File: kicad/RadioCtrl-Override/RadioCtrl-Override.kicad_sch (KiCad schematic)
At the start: 18 parts, among them J1 FW/BK/CON, J2 LF/RI/CON, J3 PJ-002AH, J5 HM10, J6 WRITER, Q1 2SC1815, Q2 2SC1815, Q3 2SC1815, Q4 2SC1815, U1 PIC16F1827-E/P

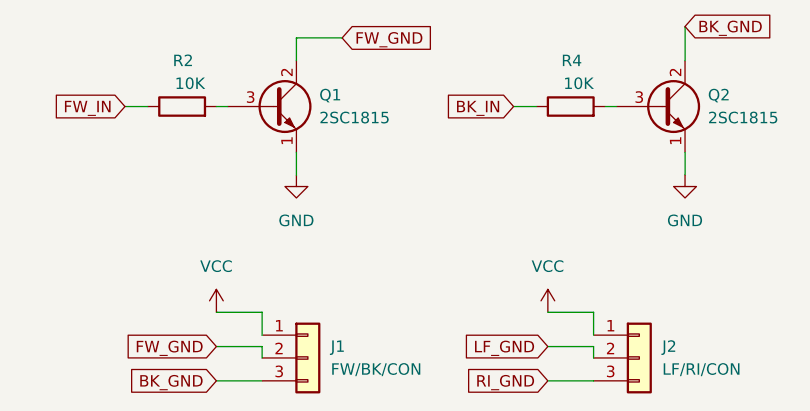
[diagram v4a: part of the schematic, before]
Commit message: 基盤の内容を修正
ターミナルのVCCをGNDに変更
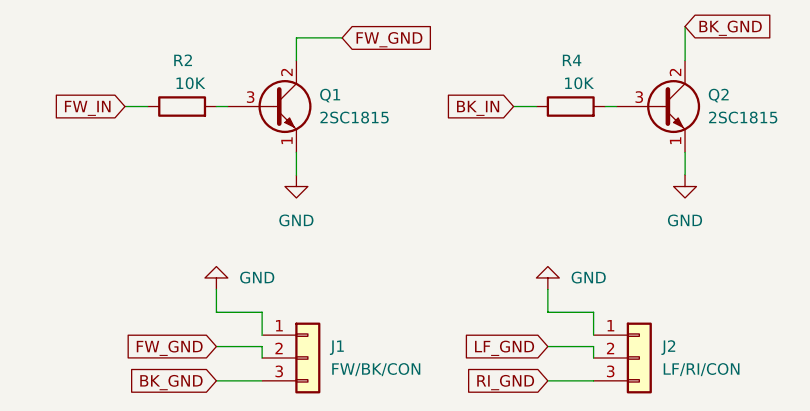
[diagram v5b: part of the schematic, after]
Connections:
- net GND: now also J1.1 (Pin_1), J2.1 (Pin_1)
- net VCC: no longer J1.1 (Pin_1), J2.1 (Pin_1)
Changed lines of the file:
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@@
+    (stroke (width 0) (type default) (color 0 0 0 0))
+  )
+  (wire (pts (xy 105.41 151.13) (xy 105.41 153.67))
     (stroke (width 0) (type default) (color 0 0 0 0))
   )
@@
   )
   (wire (pts (xy 255.27 22.86) (xy 256.54 22.86))
+    (stroke (width 0) (type default) (color 0 0 0 0))
+  )
+  (wire (pts (xy 68.58 151.13) (xy 68.58 153.67))
     (stroke (width 0) (type default) (color 0 0 0 0))
   )
@@
     (pin "5")
     (pin "6")
-  )
-  (symbol (lib_id "power:VCC") (at 105.41 153.67 0) (unit 1)
-    (in_bom yes) (on_board yes) (fields_autoplaced)
-    (property "Reference" "#PWR0104" (id 0) (at 105.41 157.48 0)
-      (effects (font (size 1.27 1.27)) hide)
-    )
-    (property "Value" "VCC" (id 1) (at 105.41 148.59 0))
-    (property "Footprint" "" (id 2) (at 105.41 153.67 0)
-      (effects (font (size 1.27 1.27)) hide)
-    )
-    (property "Datasheet" "" (id 3) (at 105.41 153.67 0)
-      (effects (font (size 1.27 1.27)) hide)
-    )
-    (pin "1")
   )
   (symbol (lib_id "power:GND") (at 77.47 138.43 0) (unit 1)
@@
     (pin "1")
   )
+  (symbol (lib_id "power:GND") (at 68.58 151.13 180) (unit 1)
+    (in_bom yes) (on_board yes) (fields_autoplaced)
+    (property "Reference" "#PWR04" (id 0) (at 68.58 144.78 0)
+      (effects (font (size 1.27 1.27)) hide)
+    )
+    (property "Value" "GND" (id 1) (at 71.12 149.8599 0)
+      (effects (font (size 1.27 1.27)) (justify right))
+    )
+    (property "Footprint" "" (id 2) (at 68.58 151.13 0)
+      (effects (font (size 1.27 1.27)) hide)
+    )
+    (property "Datasheet" "" (id 3) (at 68.58 151.13 0)
+      (effects (font (size 1.27 1.27)) hide)
+    )
+    (pin "1")
+  )
   (symbol (lib_id "power:VCC") (at 264.16 38.1 90) (unit 1)
     (in_bom yes) (on_board yes) (fields_autoplaced)
@@
     (pin "1")
   )
-  (symbol (lib_id "power:VCC") (at 68.58 153.67 0) (unit 1)
-    (in_bom yes) (on_board yes) (fields_autoplaced)
-    (property "Reference" "#PWR0103" (id 0) (at 68.58 157.48 0)
-      (effects (font (size 1.27 1.27)) hide)
-    )
-    (property "Value" "VCC" (id 1) (at 68.58 148.59 0))
-    (property "Footprint" "" (id 2) (at 68.58 153.67 0)
-      (effects (font (size 1.27 1.27)) hide)
-    )
-    (property "Datasheet" "" (id 3) (at 68.58 153.67 0)
+  (symbol (lib_id "power:GND") (at 105.41 151.13 180) (unit 1)
+    (in_bom yes) (on_board yes) (fields_autoplaced)
+    (property "Reference" "#PWR08" (id 0) (at 105.41 144.78 0)
+      (effects (font (size 1.27 1.27)) hide)
+    )
+    (property "Value" "GND" (id 1) (at 107.95 149.8599 0)
+      (effects (font (size 1.27 1.27)) (justify right))
+    )
+    (property "Footprint" "" (id 2) (at 105.41 151.13 0)
+      (effects (font (size 1.27 1.27)) hide)
+    )
+    (property "Datasheet" "" (id 3) (at 105.41 151.13 0)
       (effects (font (size 1.27 1.27)) hide)
     )
@@
       (reference "#PWR03") (unit 1) (value "VCC") (footprint "")
     )
+    (path "/745bd4b2-25a1-448c-8c0a-c204d405c6f8"
+      (reference "#PWR04") (unit 1) (value "GND") (footprint "")
+    )
     (path "/264da7a6-bef4-424f-b684-20d261d3eb2c"
       (reference "#PWR05") (unit 1) (value "GND") (footprint "")
@@
       (reference "#PWR07") (unit 1) (value "GND") (footprint "")
     )
+    (path "/8bfc5d79-50f1-47d8-be0a-48b9ef3469a4"
+      (reference "#PWR08") (unit 1) (value "GND") (footprint "")
+    )
     (path "/9752b1aa-2e1b-42c1-9333-6335b1547fb7"
       (reference "#PWR010") (unit 1) (value "GND") (footprint "")
@@
       (reference "#PWR0102") (unit 1) (value "GND") (footprint "")
     )
-    (path "/910ce226-e749-4088-a6ce-b45f093737a1"
-      (reference "#PWR0103") (unit 1) (value "VCC") (footprint "")
-    )
-    (path "/251c151d-cb9c-4431-8b51-0d8d74c512c2"
-      (reference "#PWR0104") (unit 1) (value "VCC") (footprint "")
-    )
     (path "/b1c3c639-5b8c-4507-b90f-9db0b8c30d9e"
